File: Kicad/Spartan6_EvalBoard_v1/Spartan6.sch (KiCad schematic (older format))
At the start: 25 parts, among them P401 CONN_3X2, Q401 XC6SLX16, U401 24LC64T, U402 MX25L8006E, X401 XOSC

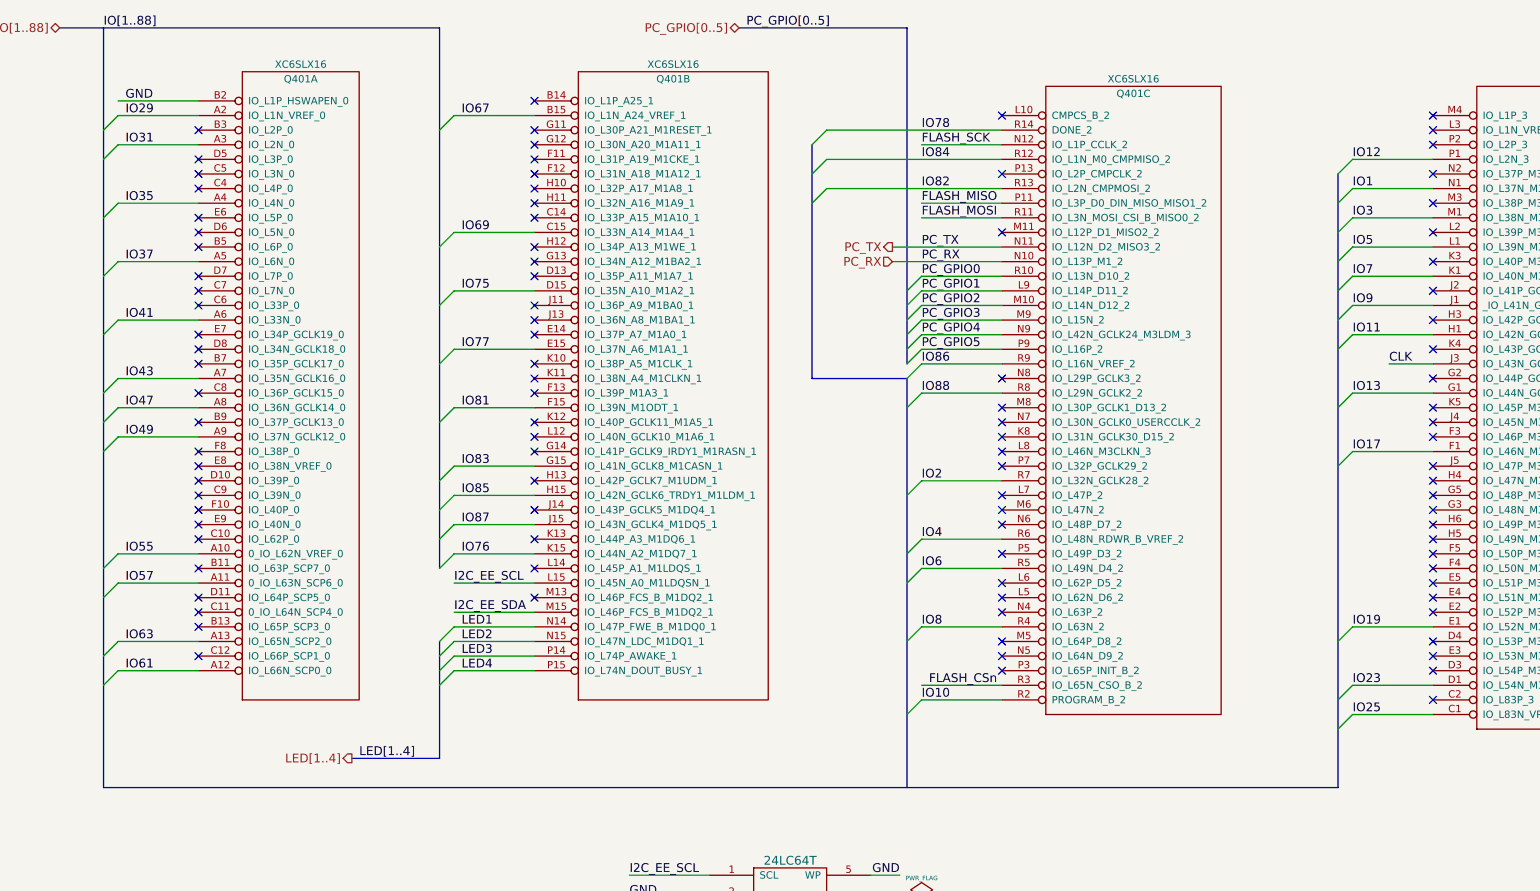
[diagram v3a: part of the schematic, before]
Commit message: BZR - Layout half done
Using LaunchPad Kicad
Layout more than half completed
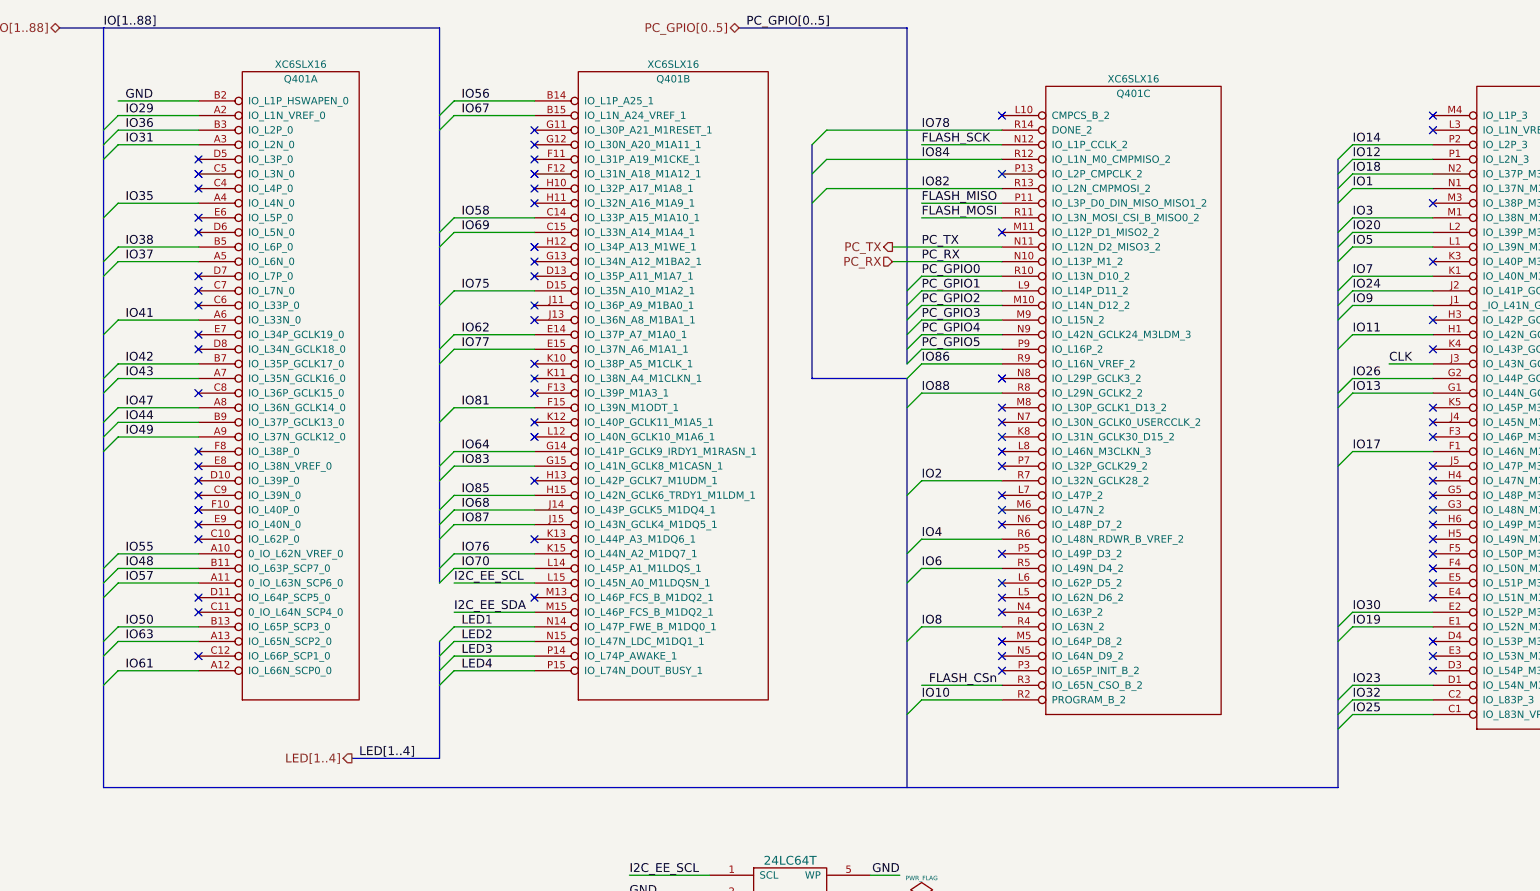
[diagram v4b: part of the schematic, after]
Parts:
- C401, C405, C406, C407, C408, C409, C410, FB401, FB402, FB403: footprint ~ -> Capacitors_SMD.pretty:C_0402
- C402, C403, C404, C411, C412, C413, C414: footprint ~ -> Capacitors_SMD.pretty:C_0603
- P401: footprint (none) -> Pin_Headers.pretty:Pin_Header_Straight_2x03
- Q401: footprint Module -> Eric.mod:CSG225
- R401, R402, R403: footprint ~ -> Resistors_SMD.pretty:R_0402
- U401: footprint (none) -> tinkerforge.mod:SOT23-5
- U402: footprint ~ -> Eric.mod:WSON8
- X401: footprint (none) -> Eric.mod:XTAL5032
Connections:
- net IO48: now reaches Q401.B11 (IO_L63P_SCP7_0)
- net IO50: now reaches Q401.B13 (IO_L65P_SCP3_0)
- net IO36: now reaches Q401.B3 (IO_L2P_0)
- net IO38: now reaches Q401.B5 (IO_L6P_0)
- net IO42: now reaches Q401.B7 (IO_L35P_GCLK17_0)
- net IO44: now reaches Q401.B9 (IO_L37P_GCLK13_0)
- net IO56: now reaches Q401.B14 (IO_L1P_A25_1)
- net IO58: now reaches Q401.C14 (IO_L33P_A15_M1A10_1)
- net IO62: now reaches Q401.E14 (IO_L37P_A7_M1A0_1)
- net IO64: now reaches Q401.G14 (IO_L41P_GCLK9_IRDY1_M1RASN_1)
- net IO68: now reaches Q401.J14 (IO_L43P_GCLK5_M1DQ4_1)
- net IO70: now reaches Q401.L14 (IO_L45P_A1_M1LDQS_1)
- net IO32: now reaches Q401.C2 (IO_L83P_3)
- net IO30: now reaches Q401.E2 (IO_L52P_M3A8_3)
- net IO26: now reaches Q401.G2 (IO_L44P_GCLK21_M3A5_3)
- net IO24: now reaches Q401.J2 (IO_L41P_GCLK27_M3DQ4_3)
- net IO20: now reaches Q401.L2 (IO_L39P_M3LDQS_3)
- net IO18: now reaches Q401.N2 (IO_L37P_M3DQ0_3)
- net IO14: now reaches Q401.P2 (IO_L2P_3)
- no-connect marks 100 -> 81
